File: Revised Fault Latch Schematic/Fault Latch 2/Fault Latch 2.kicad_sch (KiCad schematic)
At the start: 18 parts, among them J1 Inputs, K1 Fujitsu_FTR-LYAA005x, Q2 PMOS, Q3 NMOS, SW2 SW_Push_Dual_x2, U1 LM397, U2 LM397, U3 74LS279, U5 LM397, U6 74LVC1G10, U7 4N35

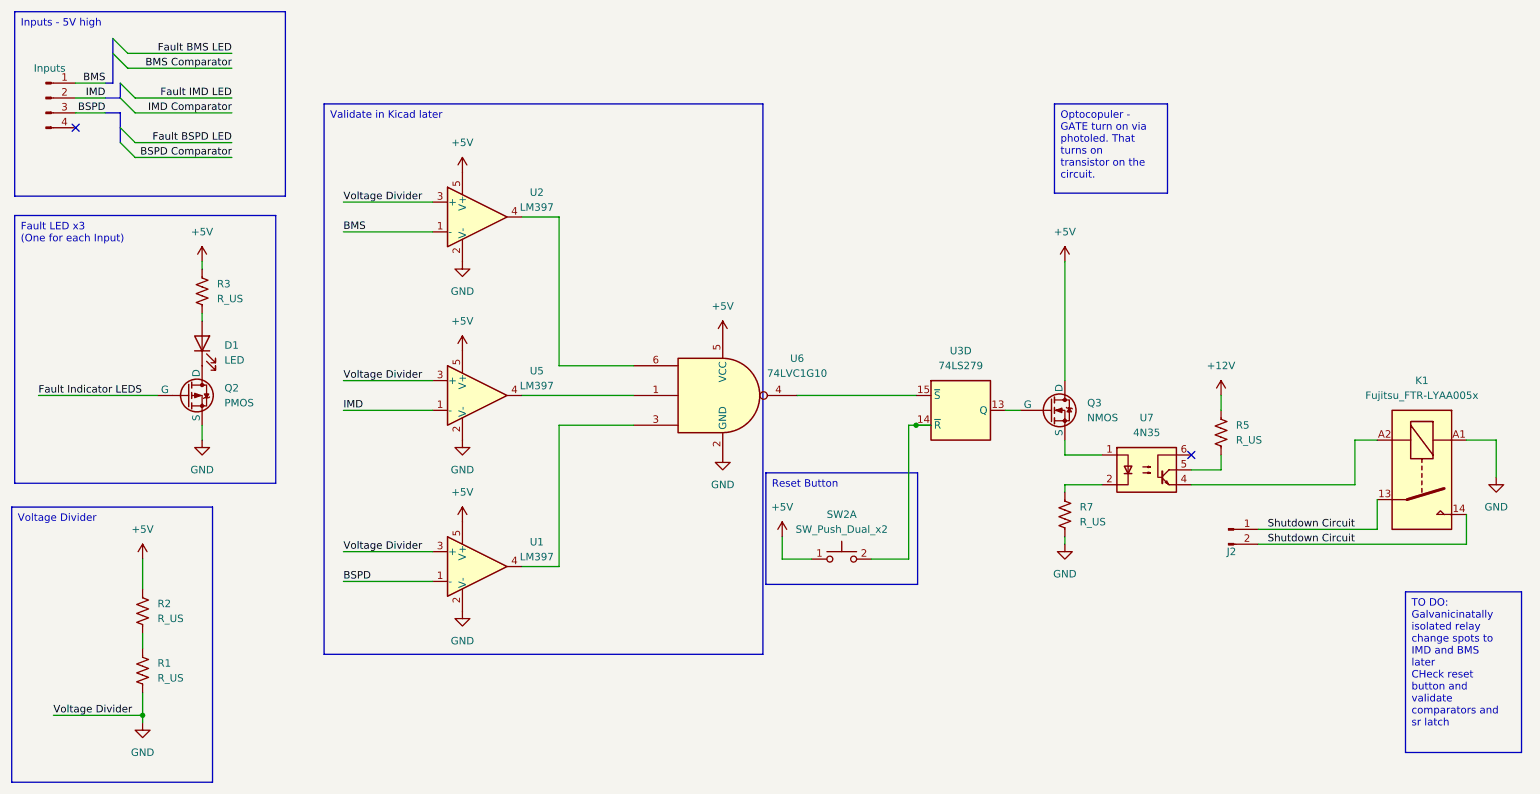
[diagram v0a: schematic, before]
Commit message: Validated Fault Latch on falstad LTspice online, and make basic RML sketch
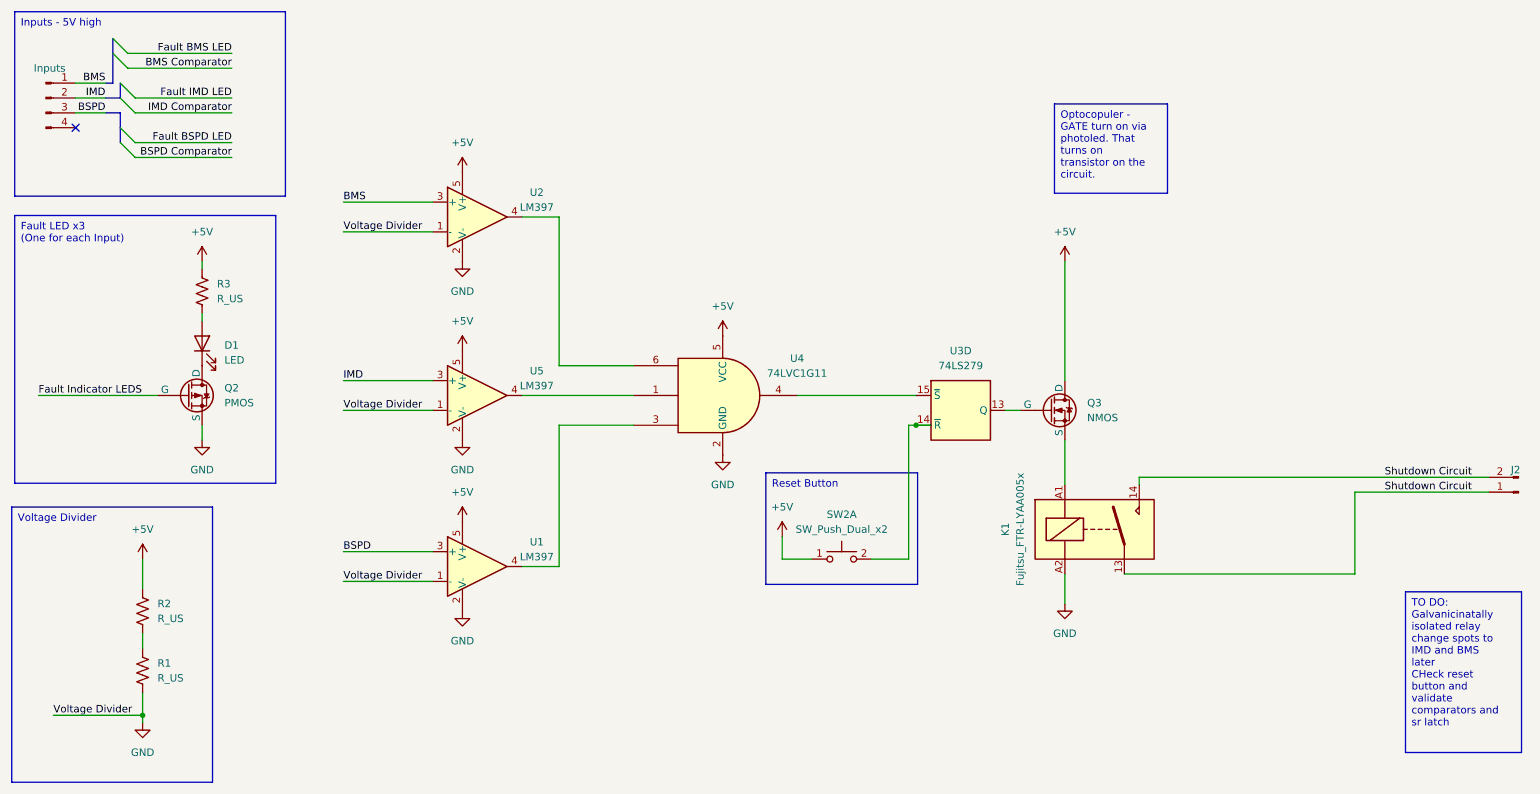
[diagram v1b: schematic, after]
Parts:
- removed R5, R7: R_US, symbol Device:R_US
- removed U6: 74LVC1G10, symbol 74xGxx:74LVC1G10
- removed U7: 4N35, Package_DIP:DIP-6_W7.62mm, symbol Isolator:4N35
- added U4: 74LVC1G11, symbol 74xGxx:74LVC1G11
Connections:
- net +5V: now also U4.5 (VCC)
- net BMS: now also U2.3 (+); no longer U2.1 (-)
- net BSPD: now also U1.3 (+); no longer U1.1 (-)
- net GND: now also K1.A2, U1.1 (-), U2.1 (-), U5.1 (-), U4.2 (GND); no longer K1.A1, U1.3 (+), U2.3 (+), U5.3 (+)
- net IMD: now also U5.3 (+); no longer U5.1 (-)
- net at U5.4: now also U4.1
- net at Q3.3 (S): now also K1.A1
- net at U2.4: now also U4.6
- net at U1.4: now also U4.3
- net at U3.15 (~{S}): now also U4.4
- no-connect marks 2 -> 1
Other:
- moved on the sheet: J2, K1
